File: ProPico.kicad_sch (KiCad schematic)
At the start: 55 parts, among them J1 USB_C_Receptacle_USB2.0, J2 SWD, J3 LEFT, J4 RIGHT, SW1 BOOTSEL, SW2 RES, U1 FM24CL16B, U2 W25Q16JVUXIQ, U3 AMS1117-3.3, U4 LM4040DBZ-3, U5 RP2040, Y1 ECS-120-12-36-AGN-TR3

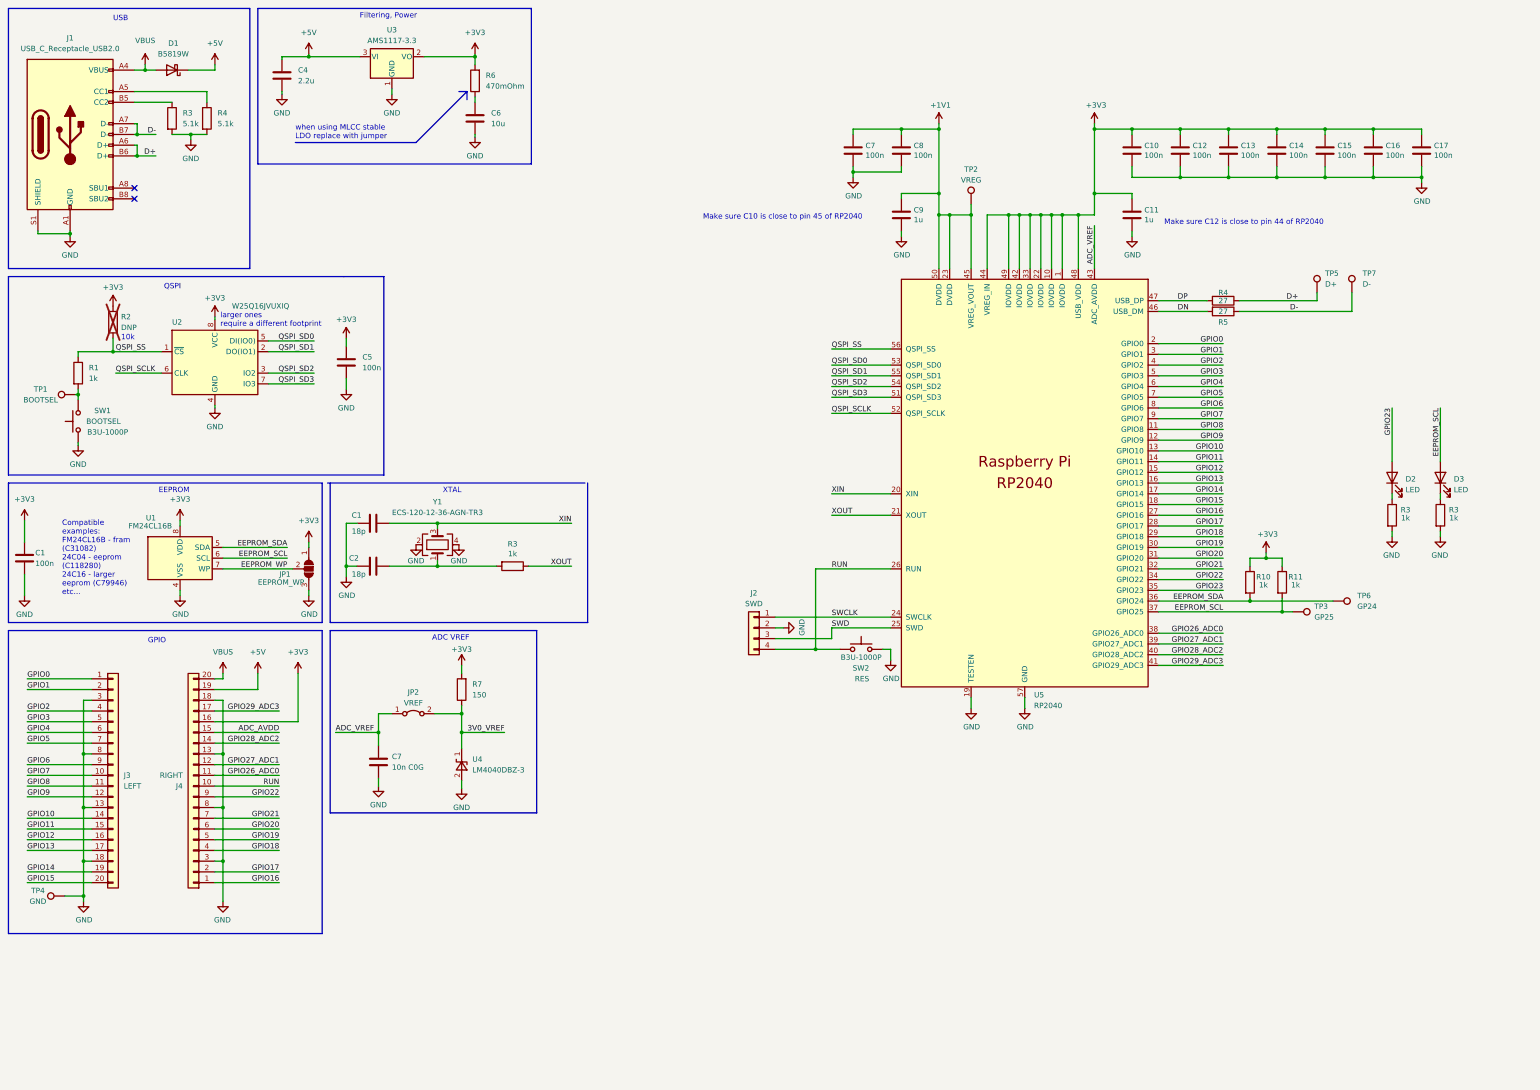
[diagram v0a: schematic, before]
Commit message: Changed LDO for lower dropout
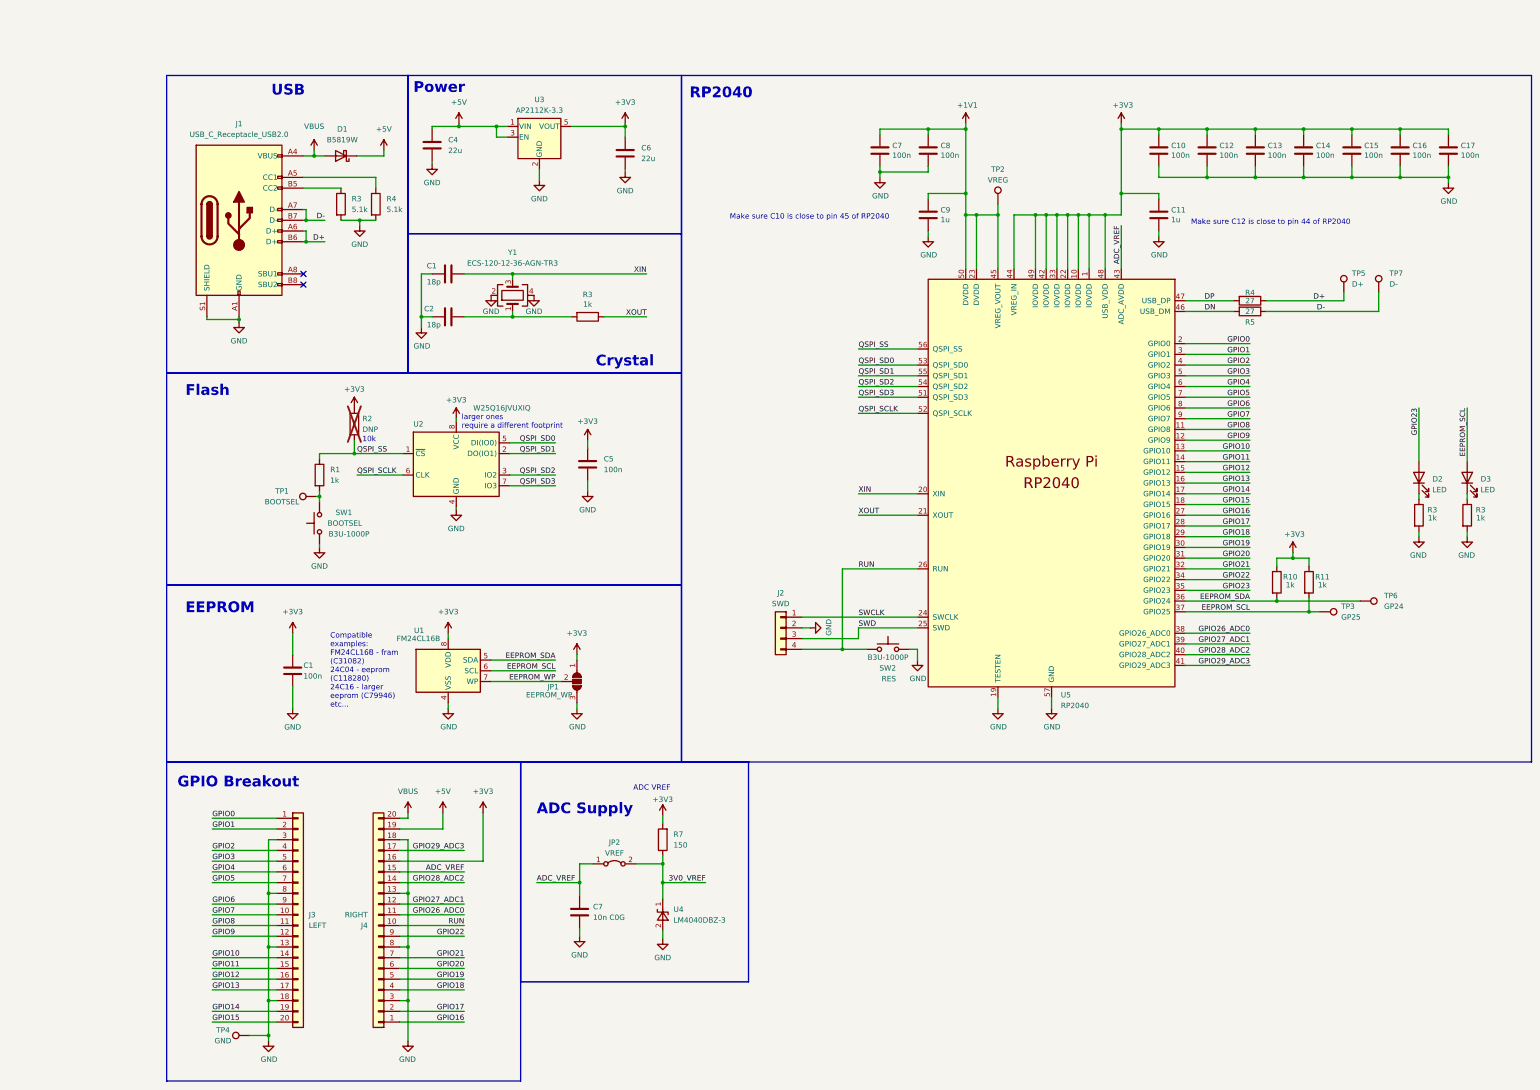
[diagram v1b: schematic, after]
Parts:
- removed R6: 470mOhm, Resistor_SMD:R_0805_2012Metric_Pad1.20x1.40mm_HandSolder, symbol Device:R
- removed U3: AMS1117-3.3, Package_TO_SOT_SMD:SOT-223-3_TabPin2, symbol Regulator_Linear:TLV1117-33
- added U3: AP2112K-3.3, Package_TO_SOT_SMD:SOT-23-5, symbol Regulator_Linear:AP2112K-3.3
- C1, C5: footprint Capacitor_SMD:C_0402_1005Metric_Pad0.74x0.62mm_HandSolder -> Capacitor_SMD:C_0402_1005Metric
- C4: value 2.2u -> 22u
- C6: value 10u -> 22u
- R1, R2, R3, R4: footprint Resistor_SMD:R_0402_1005Metric_Pad0.72x0.64mm_HandSolder -> Resistor_SMD:R_0402_1005Metric
- R7: footprint Resistor_SMD:R_0603_1608Metric_Pad0.98x0.95mm_HandSolder -> Resistor_SMD:R_0603_1608Metric
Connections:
- net ADC_AVDD is gone; now on net ADC_VREF: J4.15 (Pin_15)
- net +3V3: now also C6.1, U3.5 (VOUT)
- net +5V: now also U3.1 (VIN), U3.3 (EN)
- net GND: now also U3.2 (GND)
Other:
- note added: "ADC Supply"
- note added: "Crystal"
- note added: "Flash"
- note added: "GPIO Breakout"
- note added: "Power"
- note added: "RP2040"
- note removed: "Filtering, Power"
- note removed: "GPIO"
- note removed: "QSPI"
- note removed: "XTAL"
- note removed: "when using MLCC stable LDO replace with jumper"
- moved on the sheet: C1, C10, C11, C12, C13, C14, C15, C16, C17, C2, C4, C5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
